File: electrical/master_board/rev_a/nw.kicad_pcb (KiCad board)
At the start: 2 copper layers, 42.6 x 39.4 mm, 5 parts, among them CN70 HCSR04H;F1X4

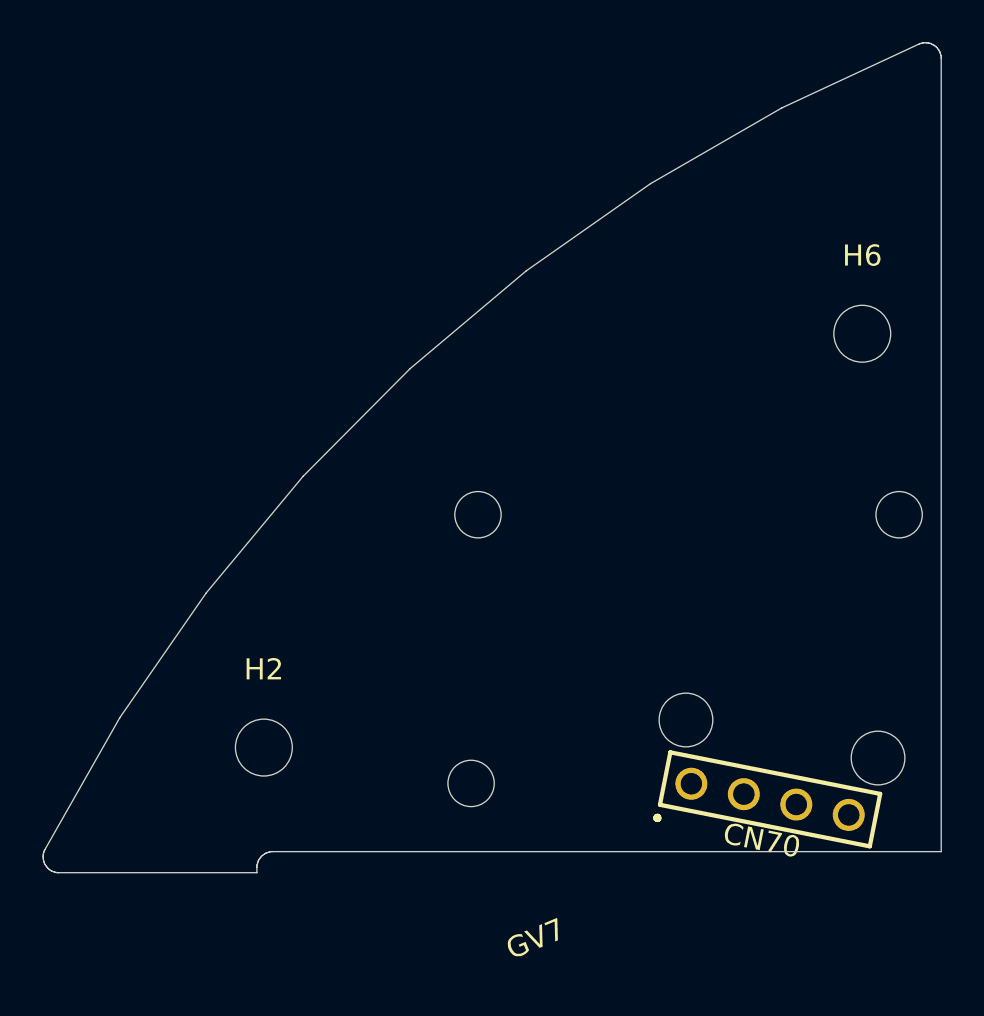
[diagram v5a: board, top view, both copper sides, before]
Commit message: Added LED's to the PCB's.
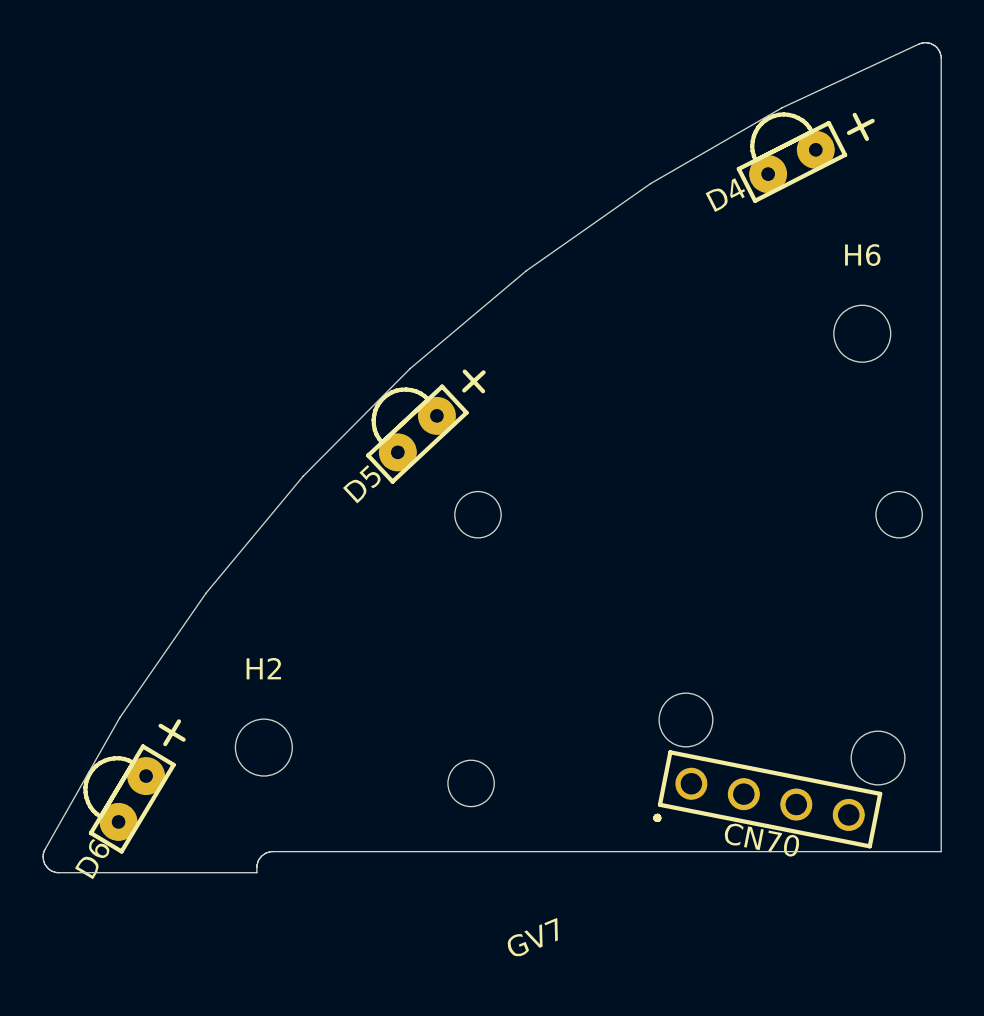
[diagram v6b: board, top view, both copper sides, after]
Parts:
- added D4: LED:GRNRA, HR2:LED_GRNRA, F.Cu at (62.9, 30.2)
- added D5: LED:GRNRA, HR2:LED_GRNRA, F.Cu at (45.1, 43.2)
- added D6: LED:GRNRA, HR2:LED_GRNRA, F.Cu at (31.6, 60.5)
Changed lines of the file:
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@@
     (tracks 0)
     (zones 0)
-    (modules 5)
+    (modules 8)
     (nets 5)
   )
@@
     (add_net "Net-(CN70-Pad4)")
   )
+  (module HR2:LED_GRNRA (layer F.Cu)
+    (at 31.584 60.5 149)
+    (fp_text reference D6 (at 0.1 -3.4 59) (layer F.SilkS)
+      (effects (font (size 1 1) (thickness 0.2)))
+    )
+    (fp_text value LED:GRNRA (at 0 0 149) (layer F.Fab)
+      (effects (font (size 1 1) (thickness 0.2)))
+    )
+    (fp_line (start -0.85 -2.4) (end 0.85 -2.4) (layer F.SilkS) (width 0.2))
+    (fp_line (start -0.85 2.4) (end -0.85 -2.4) (layer F.SilkS) (width 0.2))
+    (fp_line (start 0.85 2.4) (end -0.85 2.4) (layer F.SilkS) (width 0.2))
+    (fp_line (start 0.85 -2.4) (end 0.85 2.4) (layer F.SilkS) (width 0.2))
+    (fp_line (start 0.85 -1.5) (end 0.85 1.5) (layer F.SilkS) (width 0.2))
+    (fp_line (start 1.08 -1.48) (end 0.85 -1.5) (layer F.SilkS) (width 0.2))
+    (fp_line (start 1.31 -1.43) (end 1.08 -1.48) (layer F.SilkS) (width 0.2))
+    (fp_line (start 1.53 -1.34) (end 1.31 -1.43) (layer F.SilkS) (width 0.2))
+    (fp_line (start 1.73 -1.21) (end 1.53 -1.34) (layer F.SilkS) (width 0.2))
+    (fp_line (start 1.91 -1.06) (end 1.73 -1.21) (layer F.SilkS) (width 0.2))
+    (fp_line (start 2.06 -0.88) (end 1.91 -1.06) (layer F.SilkS) (width 0.2))
+    (fp_line (start 2.19 -0.68) (end 2.06 -0.88) (layer F.SilkS) (width 0.2))
+    (fp_line (start 2.28 -0.46) (end 2.19 -0.68) (layer F.SilkS) (width 0.2))
+    (fp_line (start 2.33 -0.23) (end 2.28 -0.46) (layer F.SilkS) (width 0.2))
+    (fp_line (start 2.35 0) (end 2.33 -0.23) (layer F.SilkS) (width 0.2))
+    (fp_line (start 2.33 0.23) (end 2.35 0) (layer F.SilkS) (width 0.2))
+    (fp_line (start 2.28 0.46) (end 2.33 0.23) (layer F.SilkS) (width 0.2))
+    (fp_line (start 2.19 0.68) (end 2.28 0.46) (layer F.SilkS) (width 0.2))
+    (fp_line (start 2.06 0.88) (end 2.19 0.68) (layer F.SilkS) (width 0.2))
+    (fp_line (start 1.91 1.06) (end 2.06 0.88) (layer F.SilkS) (width 0.2))
+    (fp_line (start 1.73 1.21) (end 1.91 1.06) (layer F.SilkS) (width 0.2))
+    (fp_line (start 1.53 1.34) (end 1.73 1.21) (layer F.SilkS) (width 0.2))
+    (fp_line (start 1.31 1.43) (end 1.53 1.34) (layer F.SilkS) (width 0.2))
+    (fp_line (start 1.08 1.48) (end 1.31 1.43) (layer F.SilkS) (width 0.2))
+    (fp_line (start 0.85 1.5) (end 1.08 1.48) (layer F.SilkS) (width 0.2))
+    (fp_line (start -0.64 3.67) (end 0.64 3.67) (layer F.SilkS) (width 0.2))
+    (fp_line (start 0 4.3) (end 0 3.04) (layer F.SilkS) (width 0.2))
+    (pad - thru_hole circle (at 0 -1.27 149) (size 1.8 1.8) (drill 0.65) (layers *.Cu *.Mask))
+    (pad + thru_hole circle (at 0 1.27 149) (size 1.8 1.8) (drill 0.65) (layers *.Cu *.Mask))
+  )
+  (module HR2:LED_GRNRA (layer F.Cu)
+    (at 45.122 43.1722 133)
+    (fp_text reference D5 (at 0 -3.5 43) (layer F.SilkS)
+      (effects (font (size 1 1) (thickness 0.2)))
+    )
+    (fp_text value LED:GRNRA (at 0 0 133) (layer F.Fab)
+      (effects (font (size 1 1) (thickness 0.2)))
+    )
+    (fp_line (start -0.85 -2.4) (end 0.85 -2.4) (layer F.SilkS) (width 0.2))
+    (fp_line (start -0.85 2.4) (end -0.85 -2.4) (layer F.SilkS) (width 0.2))
+    (fp_line (start 0.85 2.4) (end -0.85 2.4) (layer F.SilkS) (width 0.2))
+    (fp_line (start 0.85 -2.4) (end 0.85 2.4) (layer F.SilkS) (width 0.2))
+    (fp_line (start 0.85 -1.5) (end 0.85 1.5) (layer F.SilkS) (width 0.2))
+    (fp_line (start 1.08 -1.48) (end 0.85 -1.5) (layer F.SilkS) (width 0.2))
+    (fp_line (start 1.31 -1.43) (end 1.08 -1.48) (layer F.SilkS) (width 0.2))
+    (fp_line (start 1.53 -1.34) (end 1.31 -1.43) (layer F.SilkS) (width 0.2))
+    (fp_line (start 1.73 -1.21) (end 1.53 -1.34) (layer F.SilkS) (width 0.2))
+    (fp_line (start 1.91 -1.06) (end 1.73 -1.21) (layer F.SilkS) (width 0.2))
+    (fp_line (start 2.06 -0.88) (end 1.91 -1.06) (layer F.SilkS) (width 0.2))
+    (fp_line (start 2.19 -0.68) (end 2.06 -0.88) (layer F.SilkS) (width 0.2))
+    (fp_line (start 2.28 -0.46) (end 2.19 -0.68) (layer F.SilkS) (width 0.2))
+    (fp_line (start 2.33 -0.23) (end 2.28 -0.46) (layer F.SilkS) (width 0.2))
+    (fp_line (start 2.35 0) (end 2.33 -0.23) (layer F.SilkS) (width 0.2))
+    (fp_line (start 2.33 0.23) (end 2.35 0) (layer F.SilkS) (width 0.2))
+    (fp_line (start 2.28 0.46) (end 2.33 0.23) (layer F.SilkS) (width 0.2))
+    (fp_line (start 2.19 0.68) (end 2.28 0.46) (layer F.SilkS) (width 0.2))
+    (fp_line (start 2.06 0.88) (end 2.19 0.68) (layer F.SilkS) (width 0.2))
+    (fp_line (start 1.91 1.06) (end 2.06 0.88) (layer F.SilkS) (width 0.2))
+    (fp_line (start 1.73 1.21) (end 1.91 1.06) (layer F.SilkS) (width 0.2))
+    (fp_line (start 1.53 1.34) (end 1.73 1.21) (layer F.SilkS) (width 0.2))
+    (fp_line (start 1.31 1.43) (end 1.53 1.34) (layer F.SilkS) (width 0.2))
+    (fp_line (start 1.08 1.48) (end 1.31 1.43) (layer F.SilkS) (width 0.2))
+    (fp_line (start 0.85 1.5) (end 1.08 1.48) (layer F.SilkS) (width 0.2))
+    (fp_line (start -0.64 3.67) (end 0.64 3.67) (layer F.SilkS) (width 0.2))
+    (fp_line (start 0 4.3) (end 0 3.04) (layer F.SilkS) (width 0.2))
+    (pad - thru_hole circle (at 0 -1.27 133) (size 1.8 1.8) (drill 0.65) (layers *.Cu *.Mask))
+    (pad + thru_hole circle (at 0 1.27 133) (size 1.8 1.8) (drill 0.65) (layers *.Cu *.Mask))
+  )
+  (module HR2:LED_GRNRA (layer F.Cu)
+    (at 62.9117 30.2471 117)
+    (fp_text reference D4 (at 0 -3.5 27) (layer F.SilkS)
+      (effects (font (size 1 1) (thickness 0.2)))
+    )
+    (fp_text value LED:GRNRA (at 0 0 117) (layer F.Fab)
+      (effects (font (size 1 1) (thickness 0.2)))
+    )
+    (fp_line (start -0.85 -2.4) (end 0.85 -2.4) (layer F.SilkS) (width 0.2))
+    (fp_line (start -0.85 2.4) (end -0.85 -2.4) (layer F.SilkS) (width 0.2))
+    (fp_line (start 0.85 2.4) (end -0.85 2.4) (layer F.SilkS) (width 0.2))
+    (fp_line (start 0.85 -2.4) (end 0.85 2.4) (layer F.SilkS) (width 0.2))
+    (fp_line (start 0.85 -1.5) (end 0.85 1.5) (layer F.SilkS) (width 0.2))
+    (fp_line (start 1.08 -1.48) (end 0.85 -1.5) (layer F.SilkS) (width 0.2))
+    (fp_line (start 1.31 -1.43) (end 1.08 -1.48) (layer F.SilkS) (width 0.2))
+    (fp_line (start 1.53 -1.34) (end 1.31 -1.43) (layer F.SilkS) (width 0.2))
+    (fp_line (start 1.73 -1.21) (end 1.53 -1.34) (layer F.SilkS) (width 0.2))
+    (fp_line (start 1.91 -1.06) (end 1.73 -1.21) (layer F.SilkS) (width 0.2))
+    (fp_line (start 2.06 -0.88) (end 1.91 -1.06) (layer F.SilkS) (width 0.2))
+    (fp_line (start 2.19 -0.68) (end 2.06 -0.88) (layer F.SilkS) (width 0.2))
+    (fp_line (start 2.28 -0.46) (end 2.19 -0.68) (layer F.SilkS) (width 0.2))
+    (fp_line (start 2.33 -0.23) (end 2.28 -0.46) (layer F.SilkS) (width 0.2))
+    (fp_line (start 2.35 0) (end 2.33 -0.23) (layer F.SilkS) (width 0.2))
+    (fp_line (start 2.33 0.23) (end 2.35 0) (layer F.SilkS) (width 0.2))
+    (fp_line (start 2.28 0.46) (end 2.33 0.23) (layer F.SilkS) (width 0.2))
+    (fp_line (start 2.19 0.68) (end 2.28 0.46) (layer F.SilkS) (width 0.2))
+    (fp_line (start 2.06 0.88) (end 2.19 0.68) (layer F.SilkS) (width 0.2))
+    (fp_line (start 1.91 1.06) (end 2.06 0.88) (layer F.SilkS) (width 0.2))
+    (fp_line (start 1.73 1.21) (end 1.91 1.06) (layer F.SilkS) (width 0.2))
+    (fp_line (start 1.53 1.34) (end 1.73 1.21) (layer F.SilkS) (width 0.2))
+    (fp_line (start 1.31 1.43) (end 1.53 1.34) (layer F.SilkS) (width 0.2))
+    (fp_line (start 1.08 1.48) (end 1.31 1.43) (layer F.SilkS) (width 0.2))
+    (fp_line (start 0.85 1.5) (end 1.08 1.48) (layer F.SilkS) (width 0.2))
+    (fp_line (start -0.64 3.67) (end 0.64 3.67) (layer F.SilkS) (width 0.2))
+    (fp_line (start 0 4.3) (end 0 3.04) (layer F.SilkS) (width 0.2))
+    (pad - thru_hole circle (at 0 -1.27 117) (size 1.8 1.8) (drill 0.65) (layers *.Cu *.Mask))
+    (pad + thru_hole circle (at 0 1.27 117) (size 1.8 1.8) (drill 0.65) (layers *.Cu *.Mask))
+  )
   (module HR2:GROVE20x20R (layer F.Cu)

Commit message: Got Bridge connectors installed on PCB's. Tweaking still required.
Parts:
- added CN106: BRIDGE_NW_OUTER;M1x2+M2x5, HR2:BRIDGE_NW_OUTER_M1x2+M2x5, F.Cu at (49.5, 56.6)
- moved GV7 4.03 mm to (49.5, 65.5)

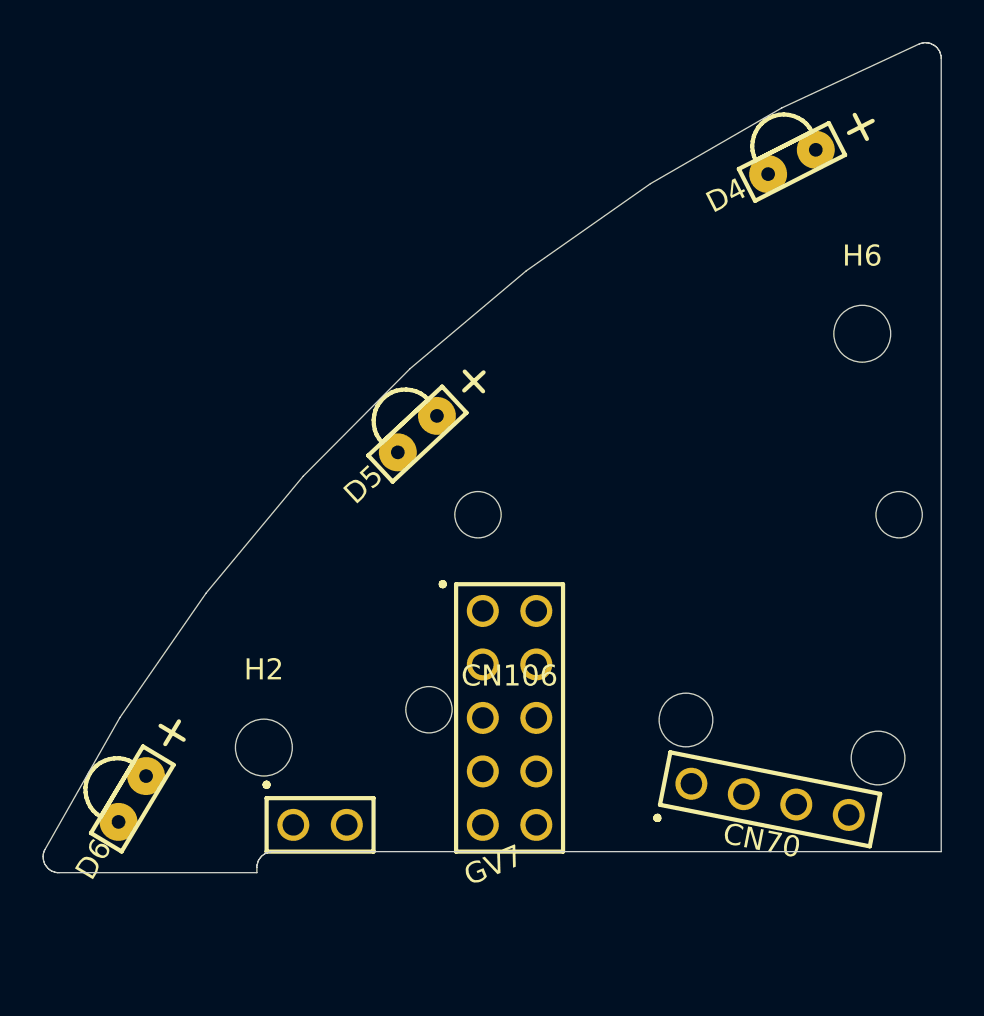
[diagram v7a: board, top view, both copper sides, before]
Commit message: The four corner boards ne/nw/se/sw are now zoned.
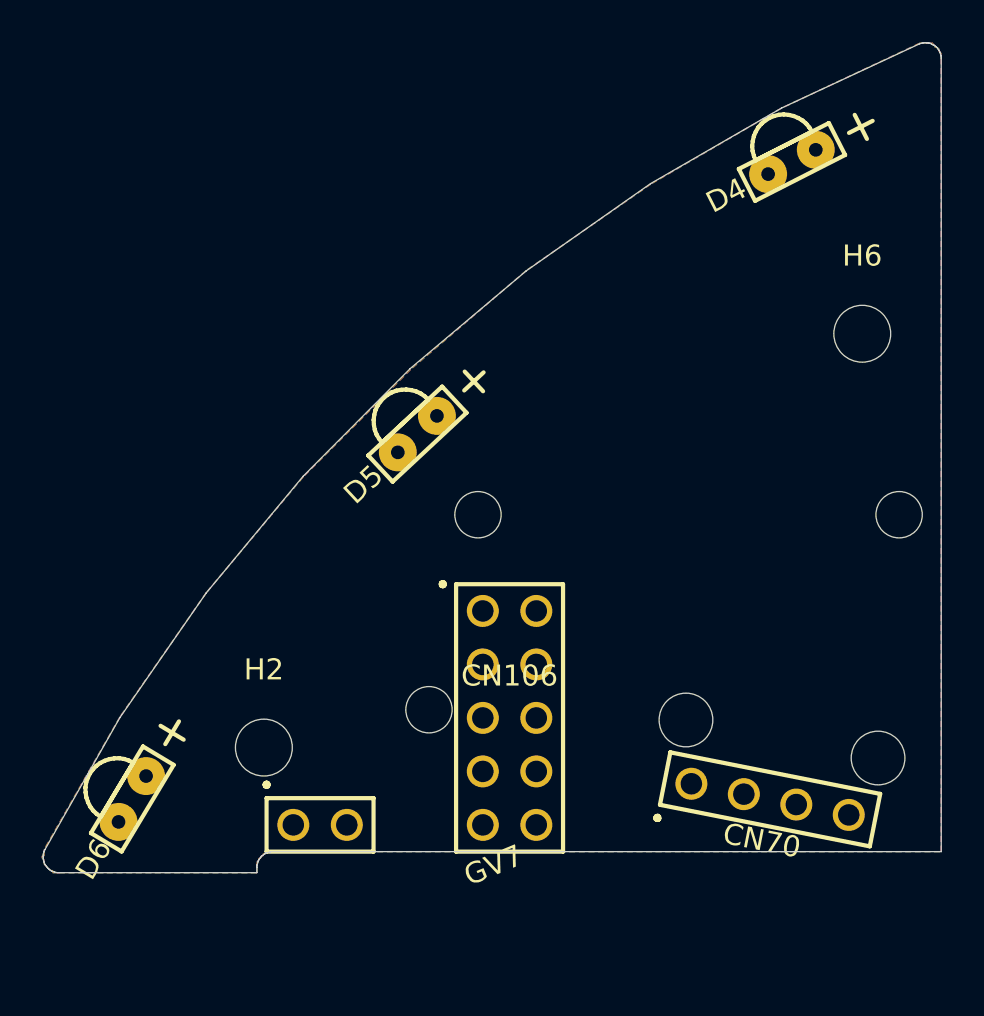
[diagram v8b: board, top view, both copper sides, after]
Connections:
- net Net-(CN106-Pad4) renamed /GND
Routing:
- added copper zone on B.Cu, net /GND
- added copper zone on F.Cu, net /GND
